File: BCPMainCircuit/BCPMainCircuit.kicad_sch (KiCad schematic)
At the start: 14 parts, among them Q1 PMOS, SW1 SW_Nidec_CAS-120A1, U1 LD1117V33, U2 Pico 2, U3 DEV-13712, U6 BME280

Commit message: Minor Changes
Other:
- note added: "Control"
- company: (none) -> TRANTOR Orbital Research Group
- title: (none) -> BCP Main Circuit
- moved on the sheet: BT1, BT2, D1, D2, D3, D4, Q1, SW1, U1, U2, U3, U5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

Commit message: Traces Run for V1
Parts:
- removed BT1: Battery, symbol Device:Battery
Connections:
- net GND: now also BT2.2 (-)
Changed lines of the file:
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@@
 	)
 	(rectangle
-		(start 100.33 21.59)
+		(start 109.22 21.59)
 		(end 191.77 45.72)
 		(stroke
@@
 	(wire
 		(pts
-			(xy 104.14 34.29) (xy 104.14 36.83)
+			(xy 115.57 34.29) (xy 115.57 36.83)
 		)
 		(stroke
@@
 	(wire
 		(pts
-			(xy 104.14 34.29) (xy 109.22 34.29)
+			(xy 115.57 34.29) (xy 123.19 34.29)
 		)
 		(stroke
@@
 		(pts
 			(xy 198.12 85.09) (xy 186.69 85.09)
-		)
-		(stroke
-			(width 0)
-			(type default)
-		)
-	)
-	(wire
-		(pts
-			(xy 119.38 34.29) (xy 123.19 34.29)
 		)
 		(stroke
@@
 	)
 	(symbol
-		(lib_id "Device:Battery")
-		(at 114.3 34.29 270)
-		(unit 1)
-		(exclude_from_sim no)
-		(in_bom yes)
-		(on_board yes)
-		(dnp no)
-		(fields_autoplaced yes)
-		(property "Reference" "BT1"
-			(at 114.8715 26.67 90)
-			(effects
-				(font
-					(size 1.27 1.27)
-				)
-			)
-		)
-		(property "Value" "Battery"
-			(at 114.8715 29.21 90)
-			(effects
-				(font
-					(size 1.27 1.27)
-				)
-			)
-		)
-		(property "Footprint" ""
-			(at 115.824 34.29 90)
-			(effects
-				(font
-					(size 1.27 1.27)
-				)
-				(hide yes)
-			)
-		)
-		(property "Datasheet" "~"
-			(at 115.824 34.29 90)
-			(effects
-				(font
-					(size 1.27 1.27)
-				)
-				(hide yes)
-			)
-		)
-		(property "Description" "Multiple-cell battery"
-			(at 114.3 34.29 0)
-			(effects
-				(font
-					(size 1.27 1.27)
-				)
-				(hide yes)
-			)
-		)
-		(pin "2"
-		)
-		(pin "1"
-		)
-		(instances
-			(project ""
-				(path "/265d59aa-caac-4c2d-9db5-2e2b992cffbc"
-					(reference "BT1")
-					(unit 1)
-				)
-			)
-		)
-	)
-	(symbol
 		(lib_id "power:GND")
 		(at 198.12 86.36 0)
@@
 	(symbol
 		(lib_id "power:GND")
-		(at 104.14 36.83 0)
+		(at 115.57 36.83 0)
 		(unit 1)
 		(exclude_from_sim no)
@@
 		(fields_autoplaced yes)
 		(property "Reference" "#PWR01"
-			(at 104.14 43.18 0)
+			(at 115.57 43.18 0)
 			(effects
 				(font
@@
 		)
 		(property "Value" "GND"
-			(at 104.14 41.91 0)
+			(at 115.57 41.91 0)
 			(effects
 				(font
@@
 		)
 		(property "Footprint" ""
-			(at 104.14 36.83 0)
+			(at 115.57 36.83 0)
 			(effects
 				(font
@@
 		)
 		(property "Datasheet" ""
-			(at 104.14 36.83 0)
+			(at 115.57 36.83 0)
 			(effects
 				(font
@@
 		)
 		(property "Description" "Power symbol creates a global label with name \"GND\" , ground"
-			(at 104.14 36.83 0)
-			(effects
-				(font
+			(at 115.57 36.83 0)
+			(effects
+				(font

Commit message: Powering the pico, whoops
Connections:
- net 3.3 V: now also U2.40 (VBUS)
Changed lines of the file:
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@@
+	(wire
+		(pts
+			(xy 186.69 80.01) (xy 193.04 80.01)
+		)
+		(stroke
+			(width 0)
+			(type default)
+		)
+	)
 	(wire
 		(pts
@@
 		)
 	)
+	(label "3.3 V"
+		(at 193.04 80.01 0)
+		(effects
+			(font
+				(size 1.27 1.27)
+			)
+			(justify left bottom)
+		)
+	)

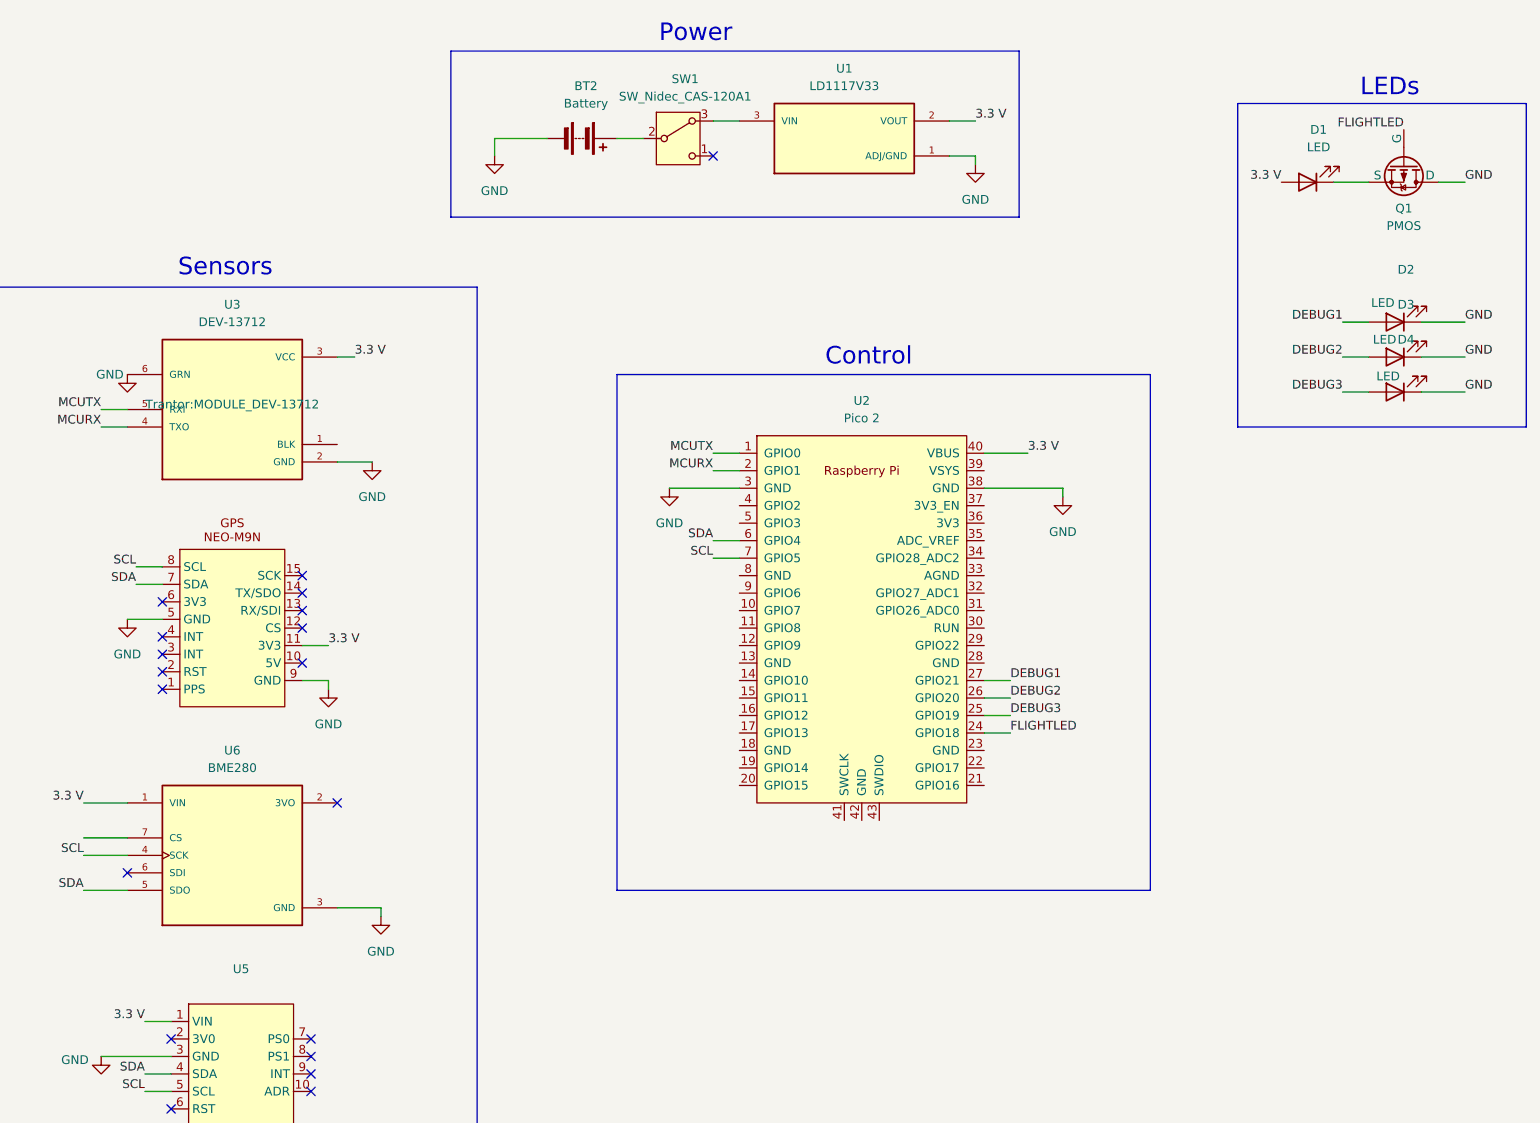
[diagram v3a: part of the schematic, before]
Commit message: Update LEDs and Silkscreen
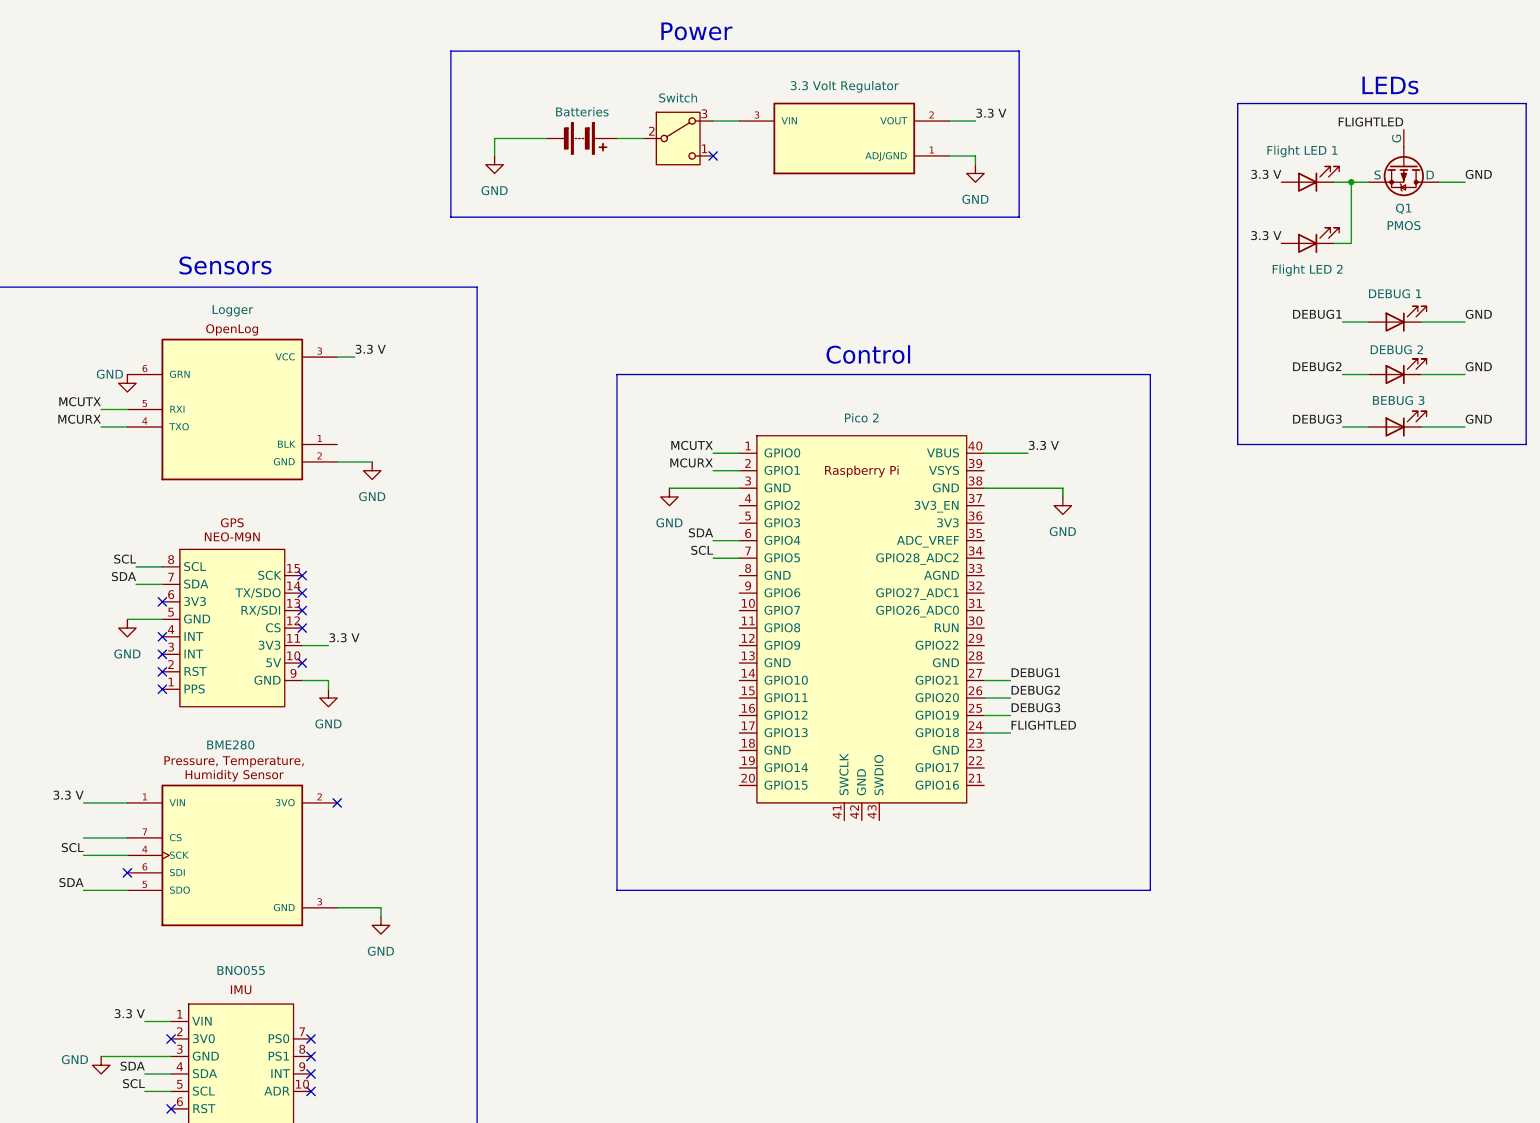
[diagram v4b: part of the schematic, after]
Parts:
- added D5: Flight LED 2, Connector_JST:JST_EH_B2B-EH-A_1x02_P2.50mm_Vertical, symbol Device:LED
- BT2: value Battery -> Batteries
- D1: value LED -> Flight LED 1; footprint (none) -> Connector_JST:JST_EH_B2B-EH-A_1x02_P2.50mm_Vertical
- D2: value LED -> DEBUG 1; footprint (none) -> LED_THT:LED_D5.0mm
- D3: value LED -> DEBUG 2; footprint (none) -> LED_THT:LED_D5.0mm
- D4: value LED -> BEBUG 3; footprint (none) -> LED_THT:LED_D5.0mm
- Q1: footprint (none) -> Package_TO_SOT_THT:TO-247-3_Vertical
- SW1: value SW_Nidec_CAS-120A1 -> Switch
- U1: value LD1117V33 -> 3.3 Volt Regulator
- U3: value DEV-13712 -> Logger
- U5: value ~ -> BNO055
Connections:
- net 3.3 V: now also D5.2 (A)
- net at D1.1 (K), Q1.3 (S): now also D5.1 (K)

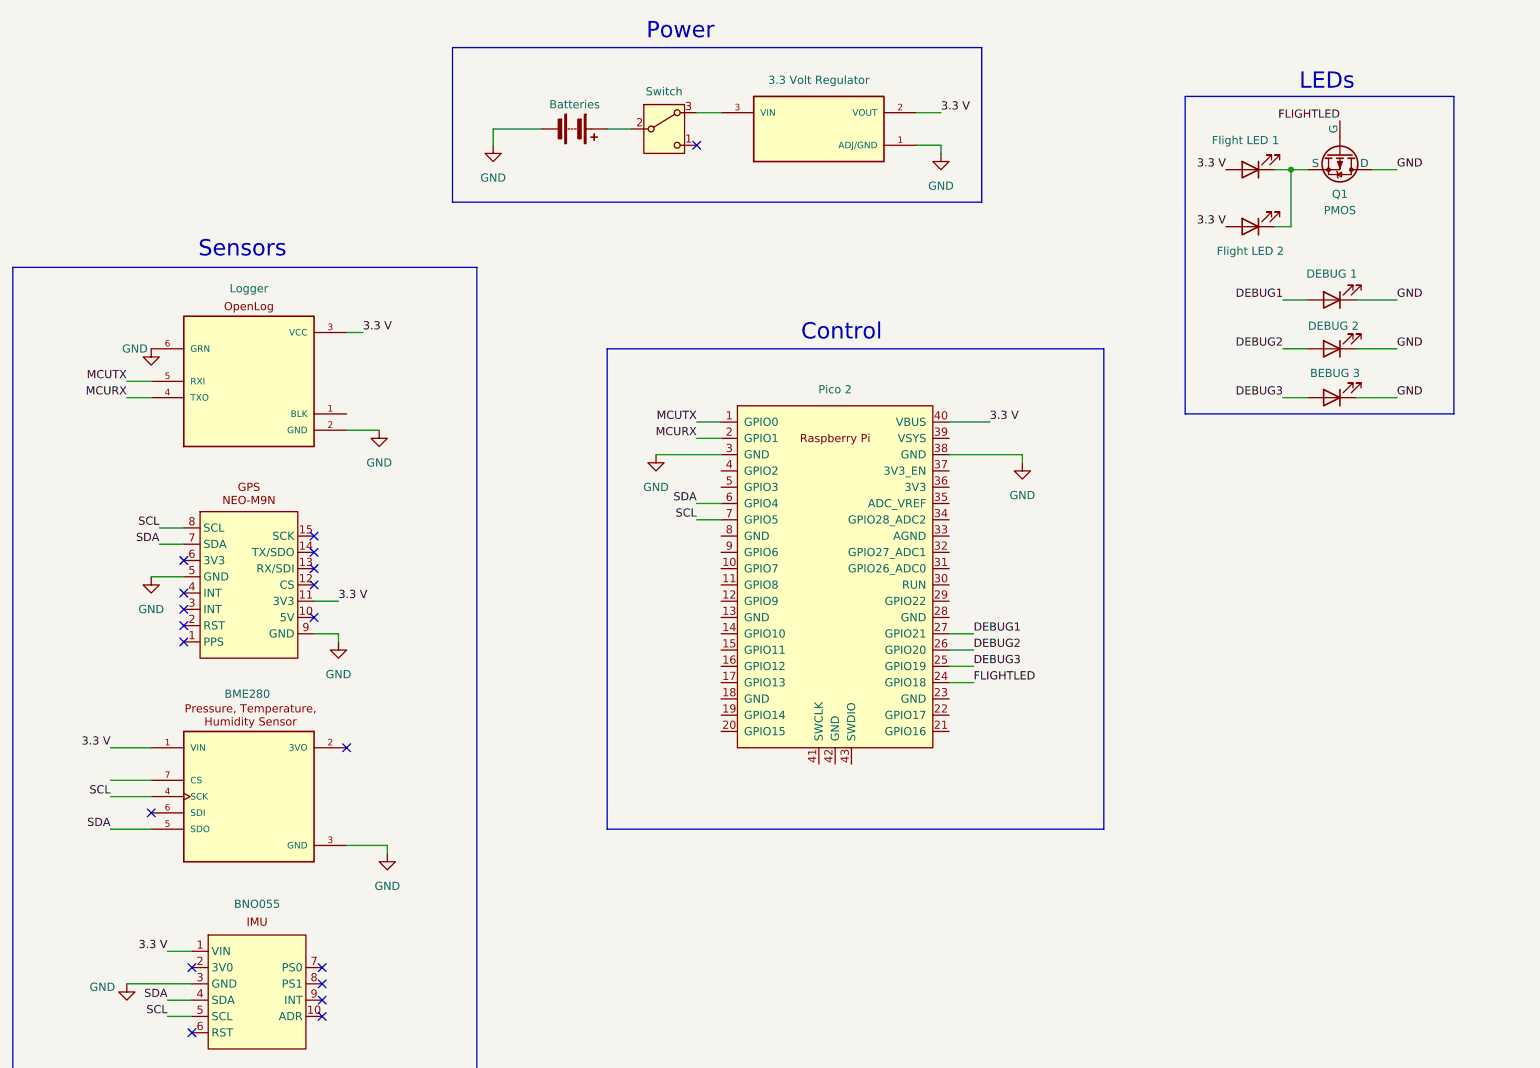
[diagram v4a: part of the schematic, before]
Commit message: Major changes: Redid traces to be thicker Moved Pico to back and rotated 180 Added resistors for LEDs (no values yet) Changed pins for flight led (i think) Changed BME280 footprint to the one we have (larger)
Minor changes:
Added caps to v.reg
Rearranged some components (freed up a good bit of space!)
Changed PMOS to NMOS
Edited footprints to better reflect actual parts/needs (assuming most parts are the same as two-month parts)
other stuff idk
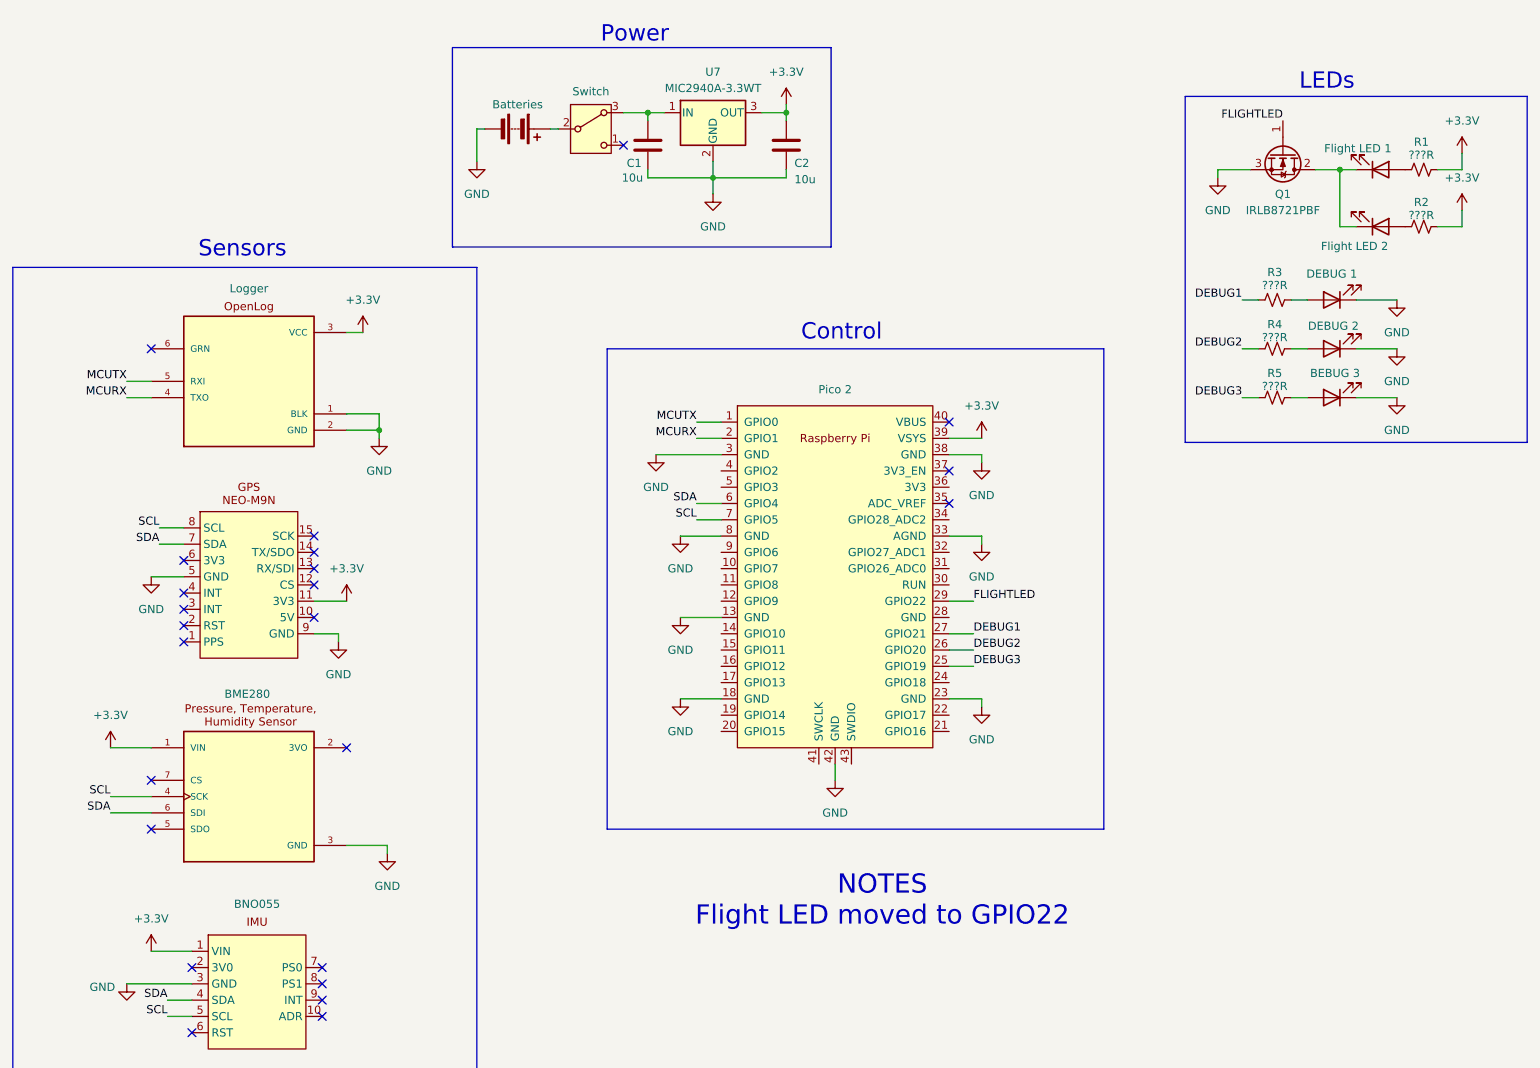
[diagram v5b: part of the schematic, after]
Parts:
- removed Q1: PMOS, Package_TO_SOT_THT:TO-247-3_Vertical, symbol Simulation_SPICE:PMOS
- removed U1: 3.3 Volt Regulator, Trantor:TO255P1020X450X1968-3, symbol Trantor:LD1117V33
- added C1, C2: 10u, Capacitor_THT:C_Disc_D7.0mm_W2.5mm_P5.00mm, symbol Device:C
- added Q1: IRLB8721PBF, Package_TO_SOT_THT:TO-220-3_Vertical, symbol Transistor_FET:IRLB8721PBF
- added R1, R2, R3, R4, R5: ???R, Resistor_THT:R_Axial_DIN0207_L6.3mm_D2.5mm_P7.62mm_Horizontal, symbol Device:R_Small_US
- added U7: MIC2940A-3.3WT, Package_TO_SOT_THT:TO-220-3_Vertical, symbol Regulator_Linear:L7805
- SW1: footprint Button_Switch_SMD:Nidec_Copal_CAS-120A -> Button_Switch_THT:SW_Slide_SPDT_Straight_CK_OS102011MS2Q
- U4: value ~ -> GPS; footprint Trantor:GPS -> Gabriel_footprints:NEO-M9N GPS
- U6: footprint Trantor:BME280 -> Gabriel_footprints:BMP280
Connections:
- net DEBUG1: now also R3.2; no longer D2.2 (A)
- net DEBUG2: now also R4.2; no longer D3.2 (A)
- net DEBUG3: now also R5.2; no longer D4.2 (A)
- net FLIGHTLED: now also U2.29 (GPIO22), Q1.1 (G); no longer U2.24 (GPIO18)
- net GND: now also U2.13 (GND), U2.18 (GND), U2.23 (GND), U2.33 (AGND), U2.42 (GND), U2.8 (GND), U3.1 (BLK), C1.2, C2.2, Q1.3 (S), U7.2 (GND); no longer U3.6 (GRN)
- net SDA: now also U6.6 (SDI); no longer U6.5 (SDO)
- net +3.3V: now reaches U2.39 (VSYS)
- net +3.3V: now also U3.3 (VCC), U4.11 (3V3), U5.1 (VIN), U6.1 (VIN), C2.1, R1.1, R2.1, U7.3 (OUT)
- net at SW1.3 (A): now also C1.1, U7.1 (IN)
- net at D1.1 (K), D5.1 (K): now also Q1.2 (D)
- removed net 3.3 V: D1.2 (A), D5.2 (A), U2.40 (VBUS), U3.3 (VCC), U4.11 (3V3), U5.1 (VIN), U6.1 (VIN)
- new net: D1.2 (A), R1.2
- new net: D4.2 (A), R5.1
- new net: D3.2 (A), R4.1
- new net: D2.2 (A), R3.1
- new net: D5.2 (A), R2.2
- no-connect marks 19 -> 24
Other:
- note added: "NOTES Flight LED moved to GPIO22"
